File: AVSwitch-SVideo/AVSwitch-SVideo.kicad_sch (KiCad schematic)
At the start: 9 parts, among them J1 Conn_01x35_Pin, J4 Mini-DIN-4, U1 SN74CBT3244PW

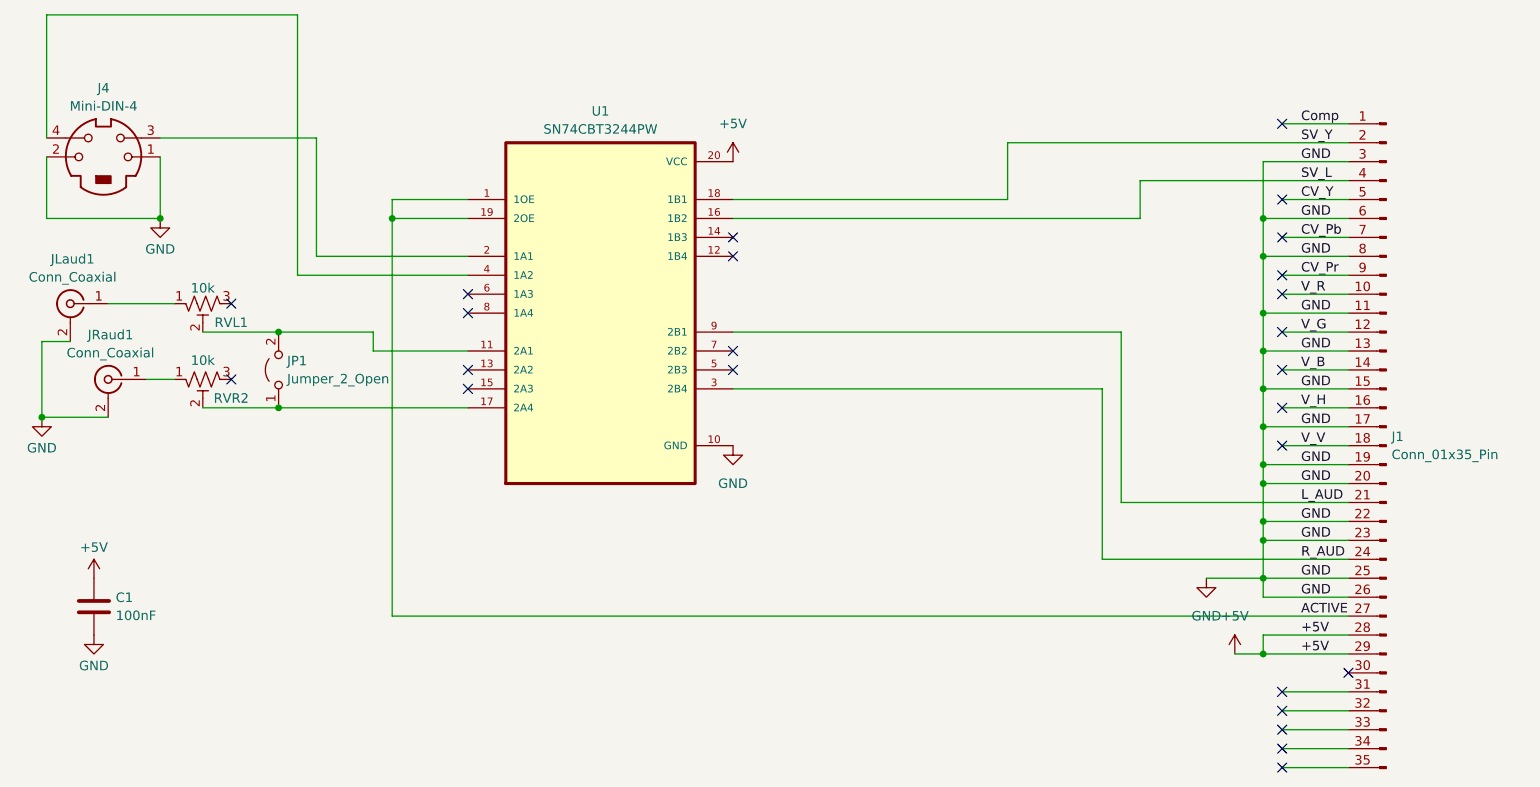
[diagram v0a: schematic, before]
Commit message: Add files via upload
New version with better footprint and ground isolation.
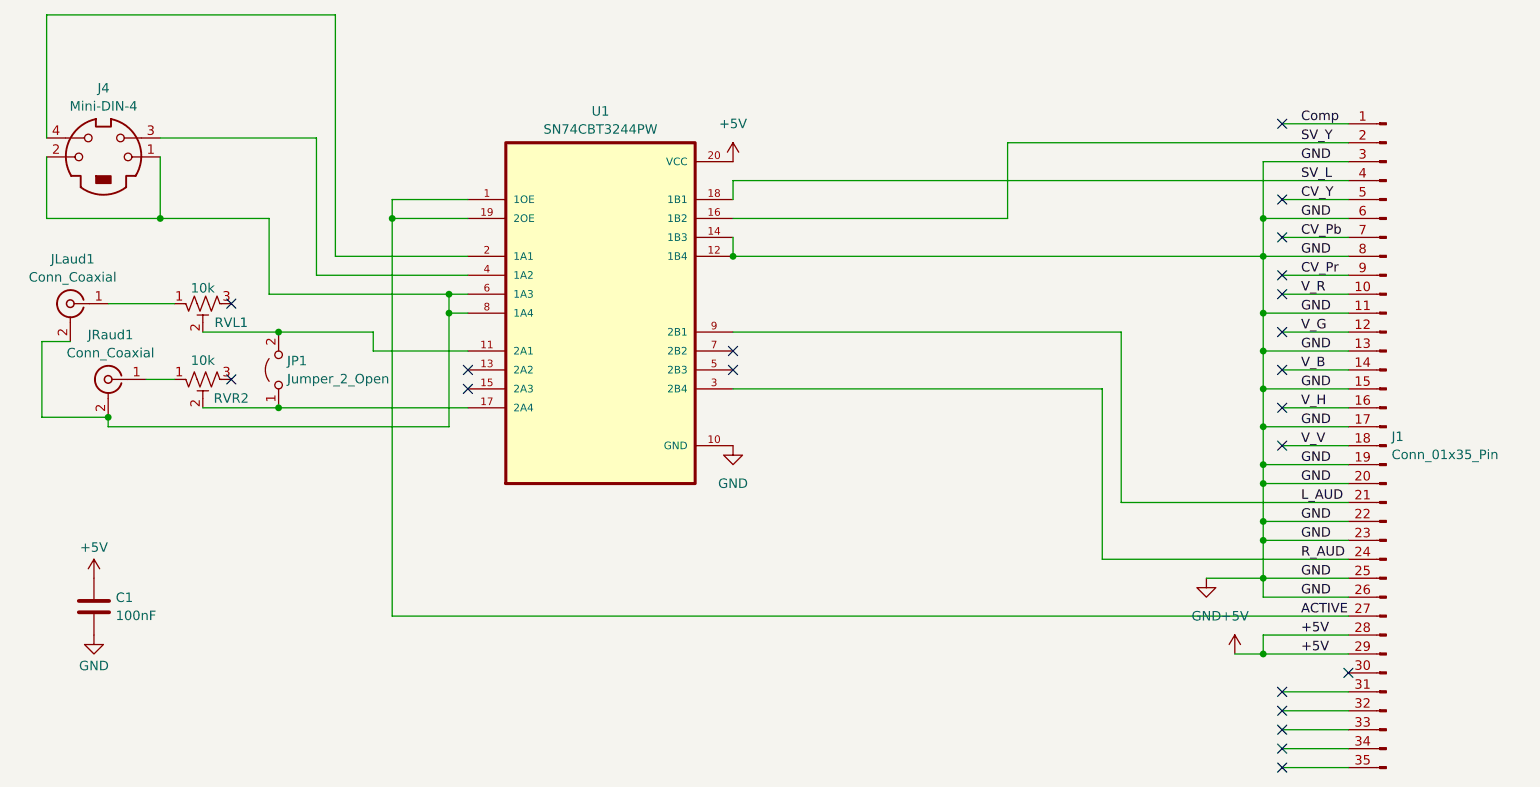
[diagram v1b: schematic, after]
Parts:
- U1: footprint Package_SO:TSSOP-20_4.4x6.5mm_P0.65mm -> Package_SO:SOIC-20W_7.5x12.8mm_P1.27mm
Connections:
- net GND: now also U1.12 (1B4), U1.14 (1B3); no longer J4.1, J4.2, JLaud1.2 (Ext), JRaud1.2 (Ext)
- net SV_L: now also U1.18 (1B1); no longer U1.16 (1B2)
- net SV_Y: now also U1.16 (1B2); no longer U1.18 (1B1)
- net at J4.3: now also U1.4 (1A2); no longer U1.2 (1A1)
- net at J4.4: now also U1.2 (1A1); no longer U1.4 (1A2)
- net at U1.6 (1A3): now also J4.1, J4.2, JLaud1.2 (Ext), JRaud1.2 (Ext), U1.8 (1A4)
- no-connect marks 25 -> 21
